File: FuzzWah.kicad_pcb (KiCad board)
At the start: 2 copper layers, 90 x 90 mm, 89 parts, among them J1 BYPASS, J2 WAH, J3 INPUT, J4 OUTPUT, J5 PWR, Q1 2N3904, Q2 2N3904, Q3 2N3904, Q4 2N3904, Q5 2N3904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

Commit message: Adctualización de PCB
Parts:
- D1, D2: footprint Diode_THT:D_DO-35_SOD27_P7.62mm_Horizontal -> DIY_jorge:D_DO-35_SOD27_P7.62mm_Horizontal
- J1, J2: moved to B.Cu
- moved J1 205.5 mm to (24.9, 114.3), turned to -90 degrees
- moved C1 189.2 mm to (27.4, 110.2), turned to 90 degrees
- moved Q1 183.1 mm to (35.6, 98.0), turned to 90 degrees
- moved Q2 181.9 mm to (32.0, 87.6), turned to 90 degrees
- moved C2 179.8 mm to (23.9, 85.1), turned to -90 degrees
- moved J2 173.4 mm to (83.8, 114.3), turned to -90 degrees
- moved C3 172.8 mm to (36.1, 91.9), turned to 90 degrees
- moved R2 172.6 mm to (27.4, 96.8), turned to -90 degrees
- moved R1 172.6 mm to (27.4, 92.7), turned to 90 degrees
- moved R101 169.7 mm to (23.9, 104.4), turned to 90 degrees
- moved R4 169.1 mm to (31.0, 104.4), turned to 90 degrees
- moved C5 168.3 mm to (41.7, 114.3)
- moved C4 166.8 mm to (41.7, 96.0), turned to -90 degrees
- moved R5 166.5 mm to (34.5, 110.7), turned to 90 degrees
- moved R3 166.3 mm to (38.1, 110.7), turned to 90 degrees
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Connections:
- SW2 pad 1: OCTAVE_IN -> OCTAVE_OUT
- SW2 pad 2: PREAMP_OUT -> TONE_IN
- SW2 pad 4: OCTAVE_OUT -> OCTAVE_IN
- SW2 pad 5: TONE_IN -> PREAMP_OUT
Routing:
- net VCC: track 0.00 -> 226.8 mm, vias 0 -> 2
- net OUTPUT: track 0.00 -> 145.5 mm
- net INPUT: track 0.00 -> 58.7 mm
- net OCTAVE_OUT: track 0.00 -> 52.7 mm
- net Net-(Q2-E): track 0.00 -> 29.8 mm
- net Net-(Q3-C): track 0.00 -> 28.1 mm
- net Net-(Q1-C): track 0.00 -> 24.7 mm
- net OCTAVE_IN: track 0.00 -> 23.8 mm
- net Net-(Q4-B): track 0.00 -> 21.9 mm
- net Net-(SW1-B): track 0.00 -> 21.7 mm
- net Net-(Q3-B): track 0.00 -> 20.8 mm
- net Net-(Q5-B): track 0.00 -> 20.6 mm
- net Net-(C3-Pad2): track 0.00 -> 20.3 mm
- net Net-(Q4-E): track 0.00 -> 18.1 mm
- net Net-(Q1-B): track 0.00 -> 16.3 mm
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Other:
- board size 90 x 90 mm -> 82 x 80 mm
- board text added: "BYPASS"
- board text added: "FXI"
- board text added: "FXO"
- board text added: "GND"
- board text added: "IN"
- board text added: "OUT"
- board text added: "VCC"
- board text added: "WAH"

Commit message: Finalización de PCB (archivos fabricación pendientes)
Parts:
- L1: footprint Inductor_THT:L_Radial_D16.8mm_P11.43mm_Vishay_IHB-1 -> Inductor_THT:L_Radial_D7.2mm_P3.00mm_Murata_1700
- moved C16 109.5 mm to (89.4, 110.5), turned to 90 degrees
- moved R31 104.5 mm to (85.9, 110.5), turned to 90 degrees
- moved Q7 103.3 mm to (91.4, 92.6), turned to 90 degrees
- moved C18 99.0 mm to (90.6, 100.2), turned to 90 degrees
- moved R32 97.9 mm to (81.0, 98.9), turned to 90 degrees
- moved Q8 96.1 mm to (96.3, 92.6), turned to 90 degrees
- moved R33 90.6 mm to (87.1, 98.9), turned to 90 degrees
- moved C17 88.8 mm to (108.5, 102.7), turned to -90 degrees
- moved R35 84.8 mm to (84.1, 91.3), turned to -90 degrees
- moved R34 79.7 mm to (101.1, 102.7), turned to 90 degrees
- moved C20 73.6 mm to (103.6, 82.1), turned to 90 degrees
- moved R37 73.1 mm to (95.0, 95.1), turned to -90 degrees
- moved L1 72.8 mm to (104.1, 88.6)
- moved C19 72.4 mm to (107.4, 82.1), turned to 90 degrees
- moved R40 68.3 mm to (98.0, 102.7), turned to 90 degrees
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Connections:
- C19 pad 1: Net-(Q7-C) -> WAH_OUT
- C19 pad 2: WAH_OUT -> Net-(Q7-C)
- R105 pad 1: Net-(D1-A) -> OCTAVE_OUT
- R105 pad 2: OCTAVE_OUT -> Net-(D1-A)
- R24 pad 1: Net-(C11-Pad2) -> Net-(SW1-C)
- R24 pad 2: Net-(SW1-C) -> Net-(C11-Pad2)
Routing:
- net WAH_OUT: track 0.00 -> 69.3 mm
- net FX_OUT: track 0.00 -> 62.5 mm
- net Net-(SW1-C): track 0.00 -> 59.8 mm
- net TONE_OUT: track 0.00 -> 46.6 mm
- net Net-(Q7-C): track 0.00 -> 45.4 mm
- net Net-(Q6-C): track 0.00 -> 26.5 mm
- net Net-(C18-Pad1): track 0.00 -> 26.1 mm
- net Net-(C17-Pad1): track 0.00 -> 25.1 mm
- net VCC: track 226.8 -> 250.3 mm
- net Net-(C4-Pad2): track 5.08 -> 26.3 mm
- net Net-(C11-Pad2): track 0.00 -> 18.4 mm
- net WAH_IN: track 0.00 -> 16.8 mm
- net TONE_IN: track 12.1 -> 28.5 mm
- net OCTAVE_OUT: track 52.7 -> 36.3 mm
- net Net-(C14-Pad1): track 0.00 -> 15.8 mm
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- added copper zone on B.Cu, net GND
- added copper zone on F.Cu, net GND
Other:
- board size 82 x 80 mm -> 75 x 75 mm

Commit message: Archivos de Fabricación listos.
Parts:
- moved R9 5.71 mm to (59.8, 71.0), turned to 90 degrees
- moved R104 4.15 mm to (62.9, 71.0), turned to 90 degrees
- moved C22 2.54 mm to (71.4, 57.1)
- moved C9 1.02 mm to (56.2, 88.8)
- moved C7 0.64 mm to (62.5, 88.8)
- moved Q3 0.51 mm to (68.8, 93.9)
- moved C11 0.36 mm to (63.3, 56.7)
- moved R102 0.26 mm to (56.2, 109.7)
- moved C6 0.23 mm to (72.7, 91.3)
- moved C5 0.18 mm to (44.5, 105.3)
- moved J3 0.15 mm to (40.0, 58.5)
- moved R12 0.13 mm to (68.5, 85.2)
- moved R13 0.13 mm to (74.5, 77.6)
- moved R14 0.13 mm to (71.5, 77.6)
- moved R6 0.13 mm to (50.2, 105.4)
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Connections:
- R9 pad 1: GND -> Net-(R9-Pad1)
- R9 pad 2: Net-(R9-Pad2) -> GND
- RV1 pad 1: Net-(R9-Pad2) -> Net-(R9-Pad1)
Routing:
- net Net-(SW1-A): track 3.56 -> 42.2 mm
- net PREAMP_OUT: track 0.00 -> 18.4 mm
- net Net-(R9-Pad1): track 0.00 -> 6.83 mm
- net Net-(R9-Pad2): track 4.91 -> 0.00 mm
- net VCC: track 250.3 -> 255.0 mm
- net Net-(Q2-E): track 34.3 -> 30.2 mm
- net TONE_IN: track 28.5 -> 32.1 mm
- net Net-(C14-Pad1): track 15.8 -> 17.3 mm
- net Net-(Q4-B): track 19.1 -> 20.1 mm
- net Net-(Q3-B): track 22.0 -> 23.0 mm
- net Net-(SW1-C): track 59.8 -> 60.4 mm

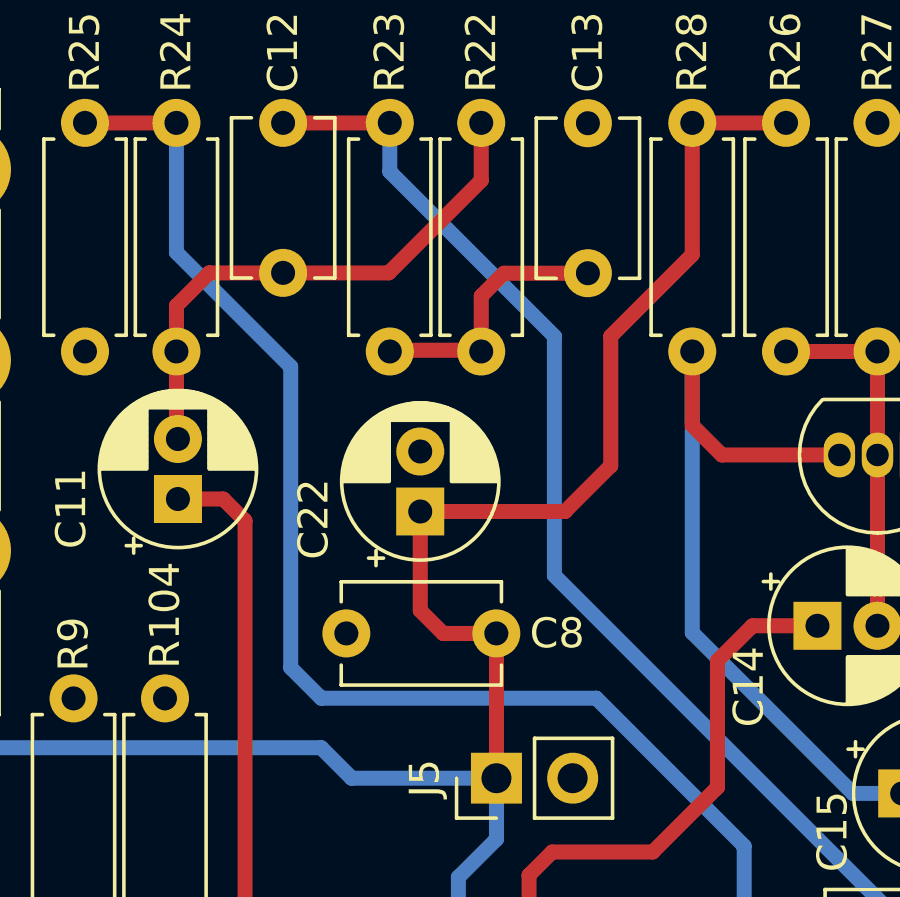
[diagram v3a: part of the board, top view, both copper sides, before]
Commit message: Finalización Archivos de Fabricación FuzzWah v1.
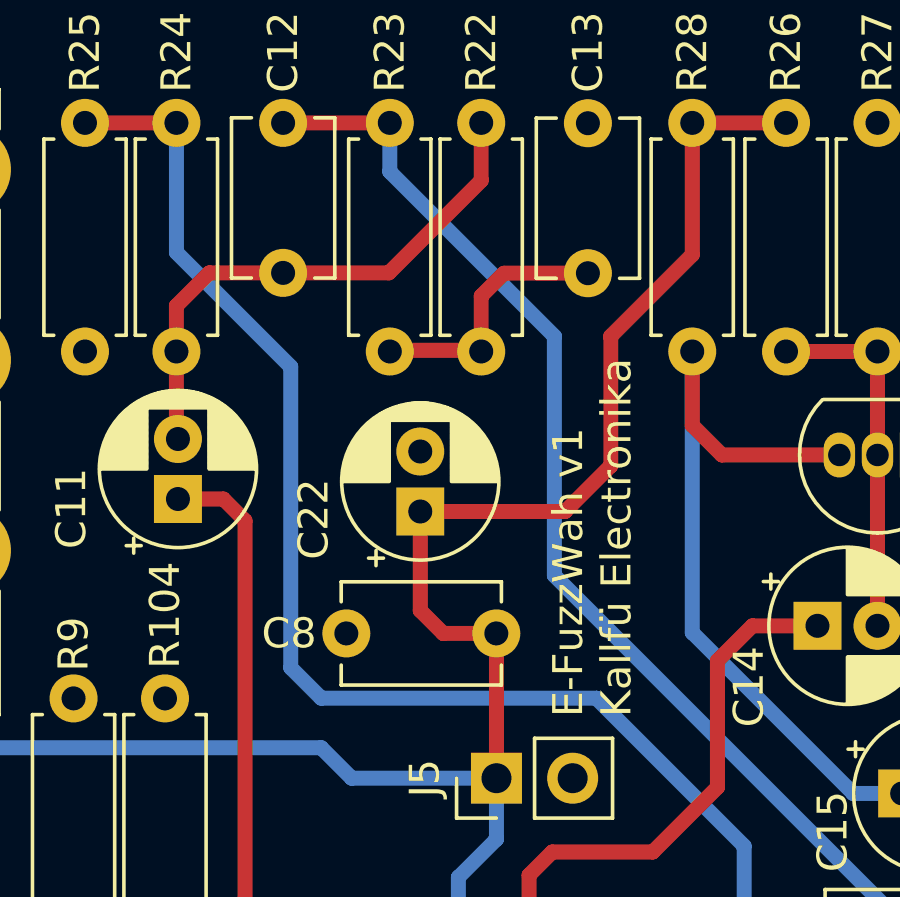
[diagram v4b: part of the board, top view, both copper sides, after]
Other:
- board text added: "E-FuzzWah v1 Kallfü Electronika"
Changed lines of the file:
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@@
 		(tags "C Disc series Radial pin pitch 5.00mm  diameter 5.1mm width 3.2mm Capacitor")
 		(property "Reference" "C8"
-			(at -2.027 0 0)
+			(at 6.909 0 0)
 			(layer "F.SilkS")
 			(effects
@@
 		)
 	)
+	(gr_text "E-FuzzWah v1\nKallfü Electronika"
+		(at 78.5 64 90)
+		(layer "F.SilkS")
+		(effects
+			(font
+				(size 1 1)
+				(thickness 0.15)
+			)
+			(justify left bottom)
+		)
+	)
 	(gr_text "IN"
 		(at 40.132 114.3 90)
@@
 		)
 	)
+	(gr_text "E-FuzzWah v1\nKallfü Electronika"
+		(at 86.5 108.8 0)
+		(layer "B.SilkS")
+		(effects
+			(font
+				(size 1.5 1.5)
+				(thickness 0.15)
+			)
+			(justify left bottom mirror)
+		)
+	)
